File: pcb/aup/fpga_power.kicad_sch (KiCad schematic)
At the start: 1 part, among them U1 XC7A50T-FGG484

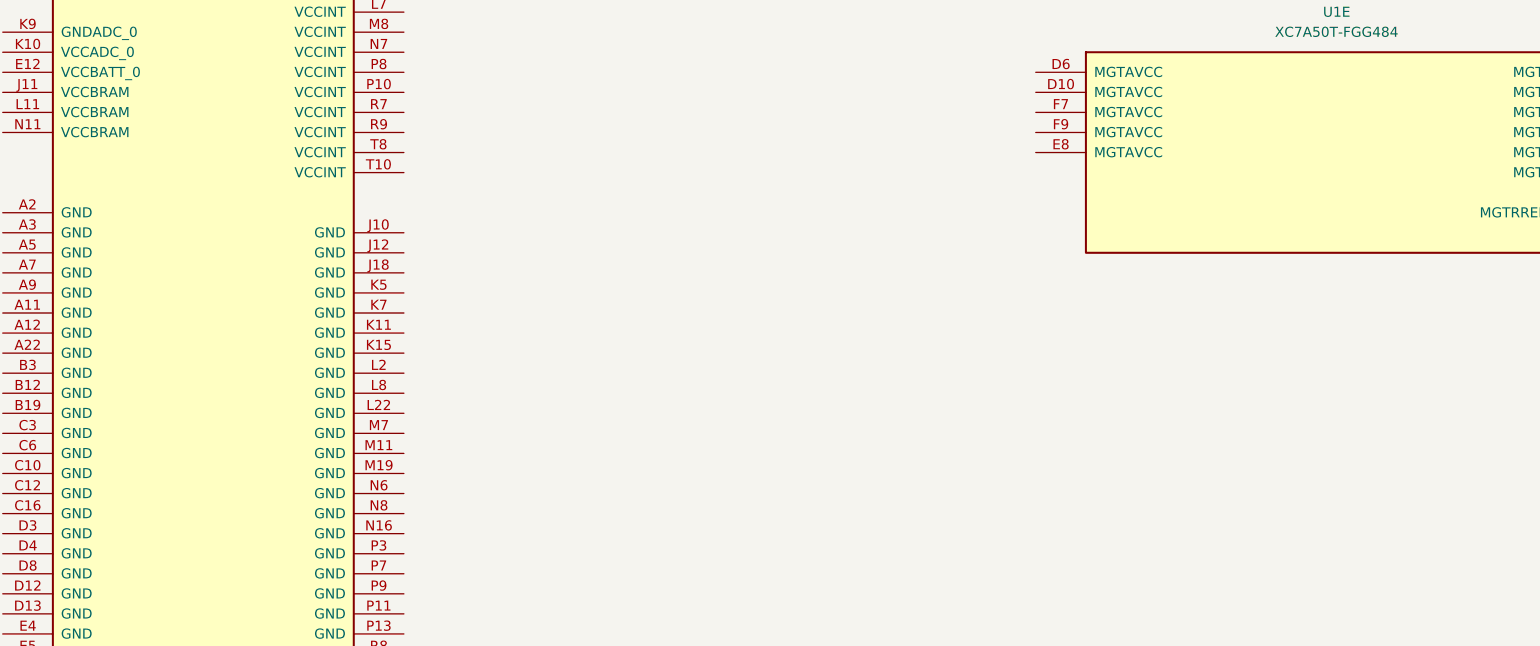
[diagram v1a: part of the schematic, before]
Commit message: Relative path fixes
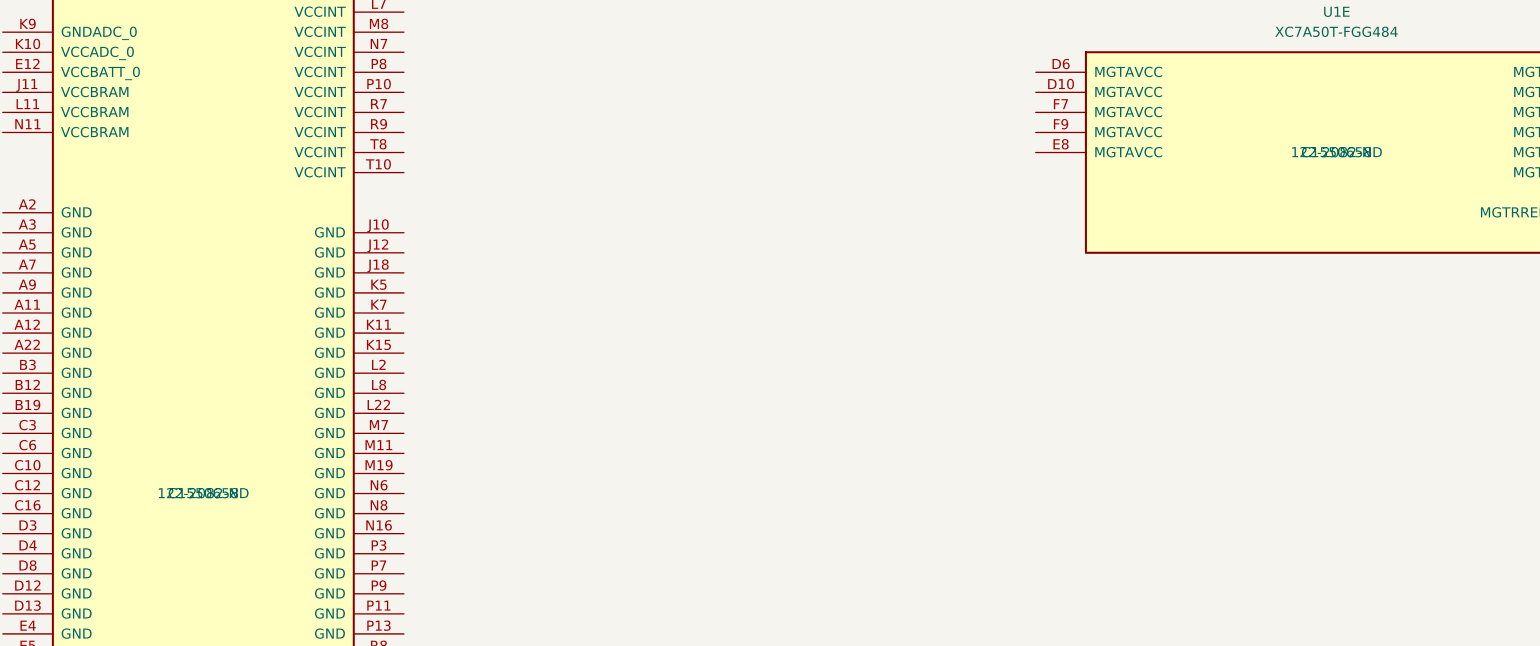
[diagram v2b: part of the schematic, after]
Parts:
- U1: footprint Package_BGA:Xilinx_FGG484 -> !Xilinx:Xilinx_FGG484; Digi-Key Part Number (none) -> 122-2082-ND; LCSC Part # (none) -> C1550658
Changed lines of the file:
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@@
 			)
 		)
-		(property "Footprint" "Package_BGA:Xilinx_FGG484"
+		(property "Footprint" "!Xilinx:Xilinx_FGG484"
 			(at 210.82 54.61 0)
 			(effects
@@
 			)
 		)
-		(property "Description" "Artix 7 T 50 XC7A50T-FGG484"
+		(property "Description" "XC7A50T-2FGG484C"
 			(at 210.82 54.61 0)
 			(effects
@@
 				)
 				(hide yes)
+			)
+		)
+		(property "LCSC Part #" "C1550658"
+			(at 210.82 54.61 0)
+			(effects
+				(font
+					(size 1.27 1.27)
+				)
+			)
+		)
+		(property "Digi-Key Part Number" "122-2082-ND"
+			(at 210.82 54.61 0)
+			(effects
+				(font
+					(size 1.27 1.27)
+				)
 			)
 		)
@@
 			)
 		)
-		(property "Footprint" "Package_BGA:Xilinx_FGG484"
+		(property "Footprint" "!Xilinx:Xilinx_FGG484"
 			(at 67.31 97.79 0)
 			(effects
@@
 			)
 		)
-		(property "Description" "Artix 7 T 50 XC7A50T-FGG484"
+		(property "Description" "XC7A50T-2FGG484C"
 			(at 67.31 97.79 0)
 			(effects
@@
 			)
 		)
+		(property "LCSC Part #" "C1550658"
+			(at 67.31 97.79 0)
+			(effects
+				(font
+					(size 1.27 1.27)
+				)
+			)
+		)
+		(property "Digi-Key Part Number" "122-2082-ND"
+			(at 67.31 97.79 0)
+			(effects
+				(font
+					(size 1.27 1.27)
+				)
+			)
+		)

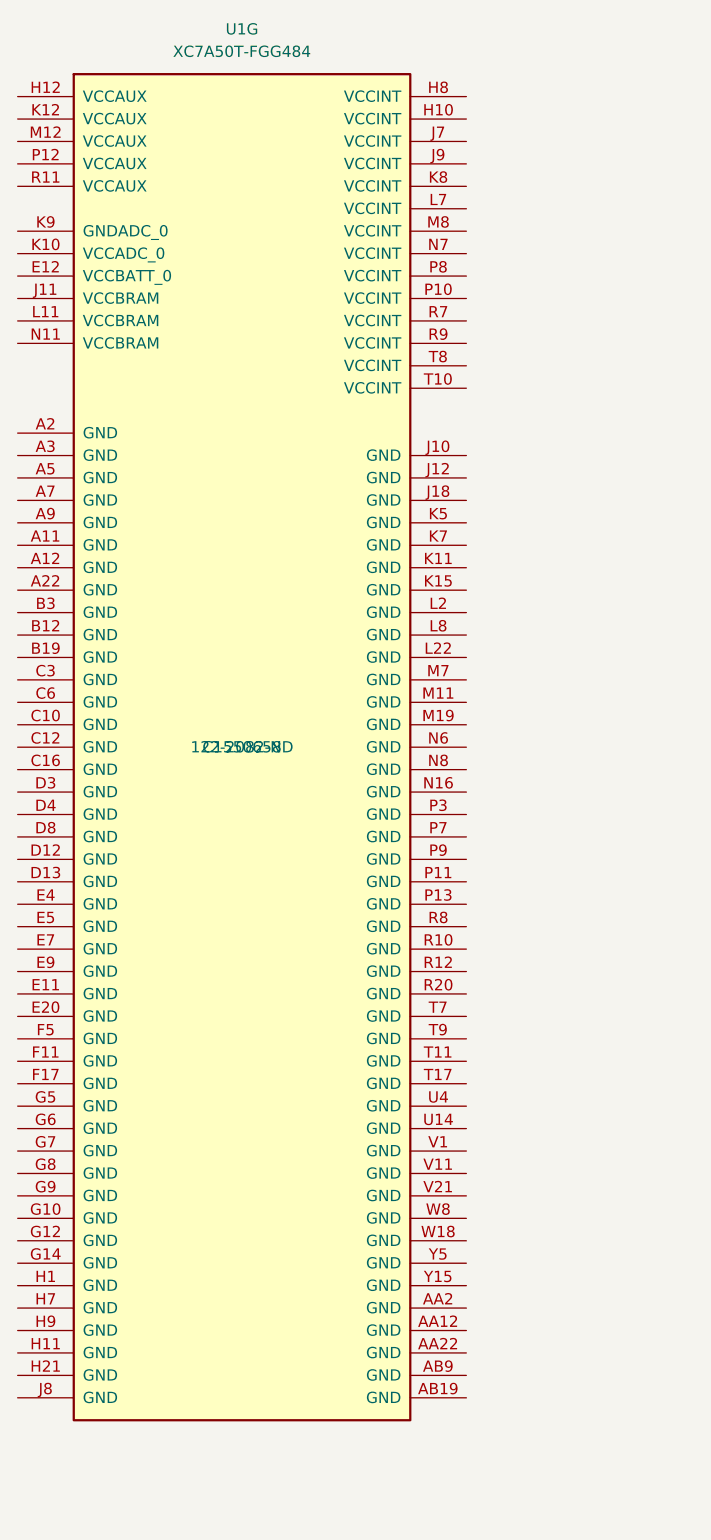
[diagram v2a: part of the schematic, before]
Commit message: Add some todo's on schematic. Add vias to fpga
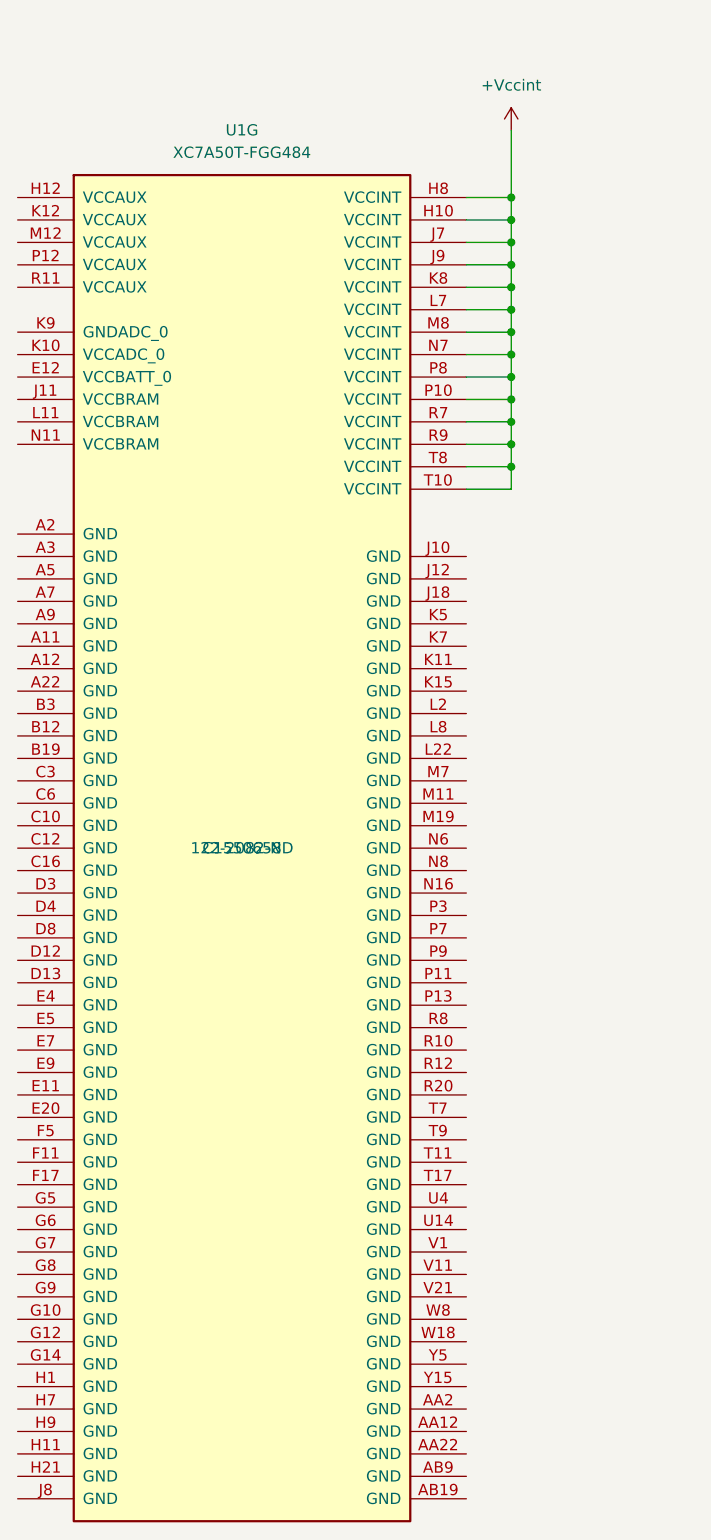
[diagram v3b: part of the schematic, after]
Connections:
- net +Vccint: now reaches U1.H10 (VCCINT)
- net +Vccint: now also U1.H8 (VCCINT), U1.J7 (VCCINT), U1.J9 (VCCINT), U1.K8 (VCCINT), U1.L7 (VCCINT), U1.M8 (VCCINT), U1.N7 (VCCINT), U1.P10 (VCCINT), U1.P8 (VCCINT), U1.R7 (VCCINT), U1.R9 (VCCINT), U1.T10 (VCCINT), U1.T8 (VCCINT)
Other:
- moved on the sheet: U1G

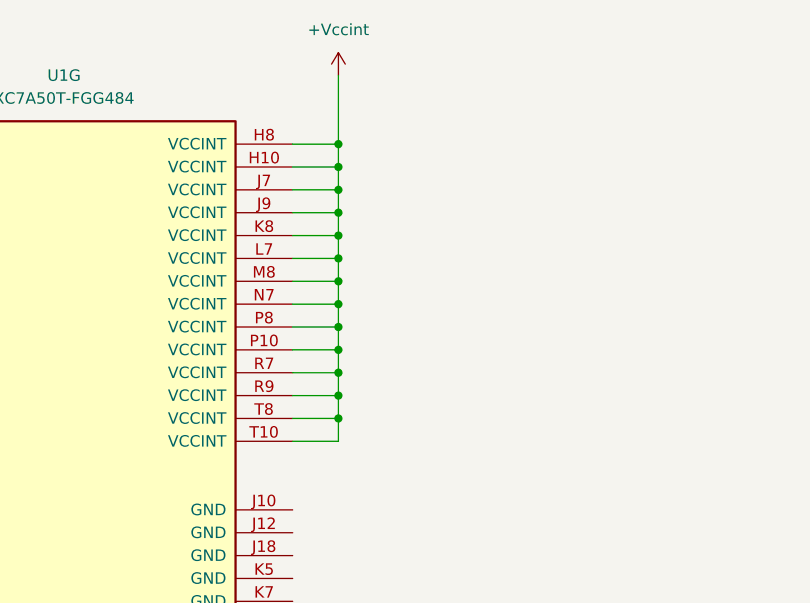
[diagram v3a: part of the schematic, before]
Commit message: Start to add net class color
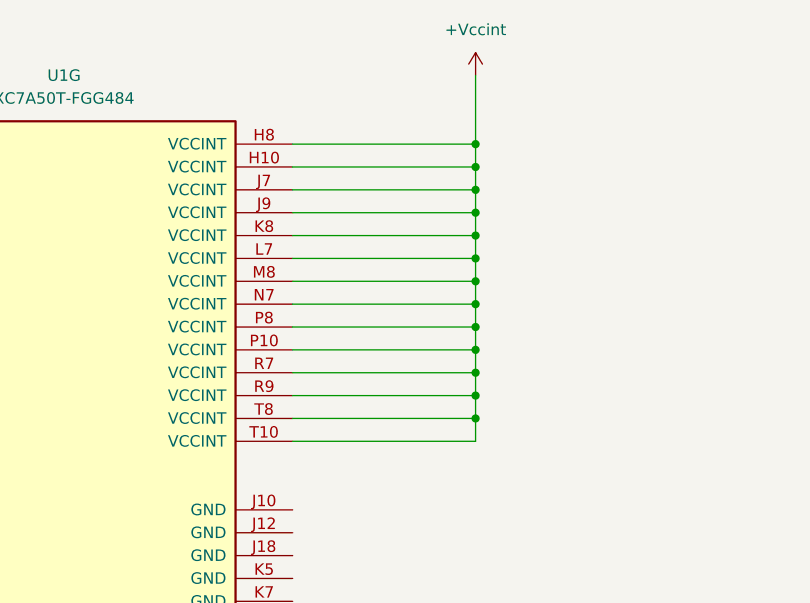
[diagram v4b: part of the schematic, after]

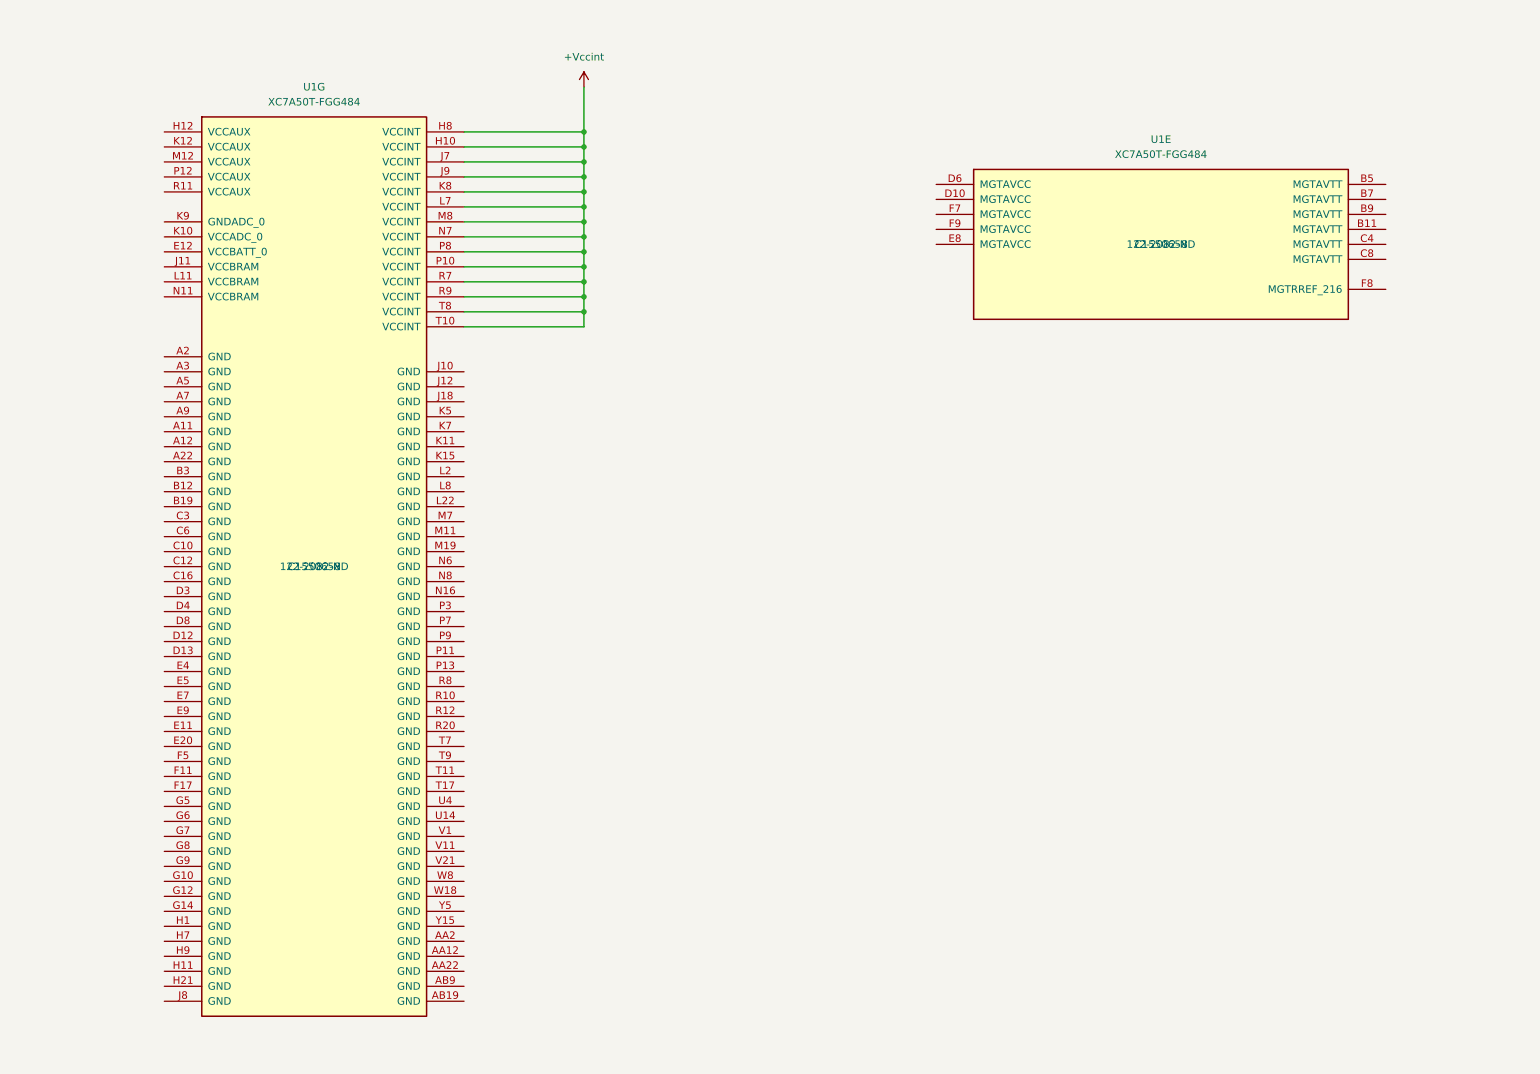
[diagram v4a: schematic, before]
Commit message: Add netnames for rails
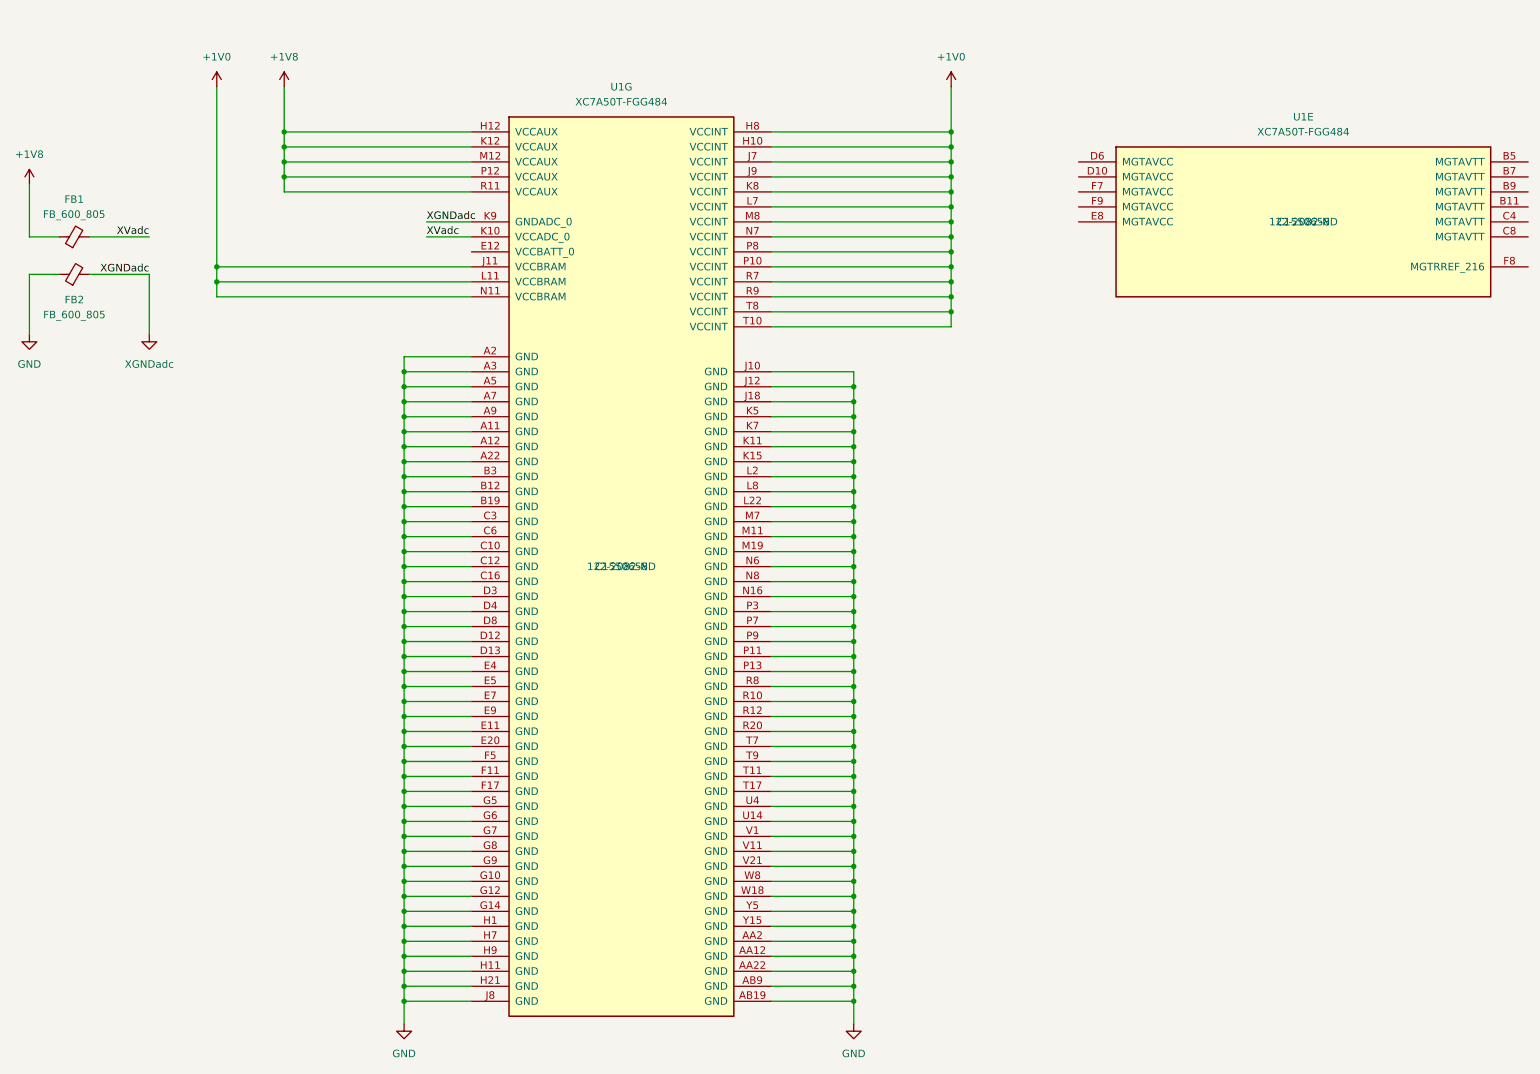
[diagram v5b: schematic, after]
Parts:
- added FB1, FB2: FB_600_805, Inductor_SMD:L_0805_2012Metric, symbol !Misc:FB_600
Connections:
- net +Vccint is gone; now on net +1V0: U1.H10 (VCCINT), U1.H8 (VCCINT), U1.J7 (VCCINT), U1.J9 (VCCINT), U1.K8 (VCCINT), U1.L7 (VCCINT), U1.M8 (VCCINT), U1.N7 (VCCINT), U1.P10 (VCCINT), U1.P8 (VCCINT), U1.R7 (VCCINT), U1.R9 (VCCINT), U1.T10 (VCCINT), U1.T8 (VCCINT)
- net GND: now reaches U1.A11 (GND)
- net GND: now also U1.A12 (GND), U1.A2 (GND), U1.A22 (GND), U1.A3 (GND), U1.A5 (GND), U1.A7 (GND), U1.A9 (GND), U1.AA12 (GND), U1.AA2 (GND), U1.AA22 (GND), U1.AB19 (GND), U1.AB9 (GND), U1.B12 (GND), U1.B19 (GND), U1.B3 (GND), U1.C10 (GND), U1.C12 (GND), U1.C16 (GND), U1.C3 (GND), U1.C6 (GND), U1.D12 (GND), U1.D13 (GND), U1.D3 (GND), U1.D4 (GND), U1.D8 (GND), U1.E11 (GND), U1.E20 (GND), U1.E4 (GND), U1.E5 (GND), U1.E7 (GND), U1.E9 (GND), U1.F11 (GND), U1.F17 (GND), U1.F5 (GND), U1.G10 (GND), U1.G12 (GND), U1.G14 (GND), U1.G5 (GND), U1.G6 (GND), U1.G7 (GND), U1.G8 (GND), U1.G9 (GND), U1.H1 (GND), U1.H11 (GND), U1.H21 (GND), U1.H7 (GND), U1.H9 (GND), U1.J10 (GND), U1.J12 (GND), U1.J18 (GND), U1.J8 (GND), U1.K11 (GND), U1.K15 (GND), U1.K5 (GND), U1.K7 (GND), U1.L2 (GND), U1.L22 (GND), U1.L8 (GND), U1.M11 (GND), U1.M19 (GND), U1.M7 (GND), U1.N16 (GND), U1.N6 (GND), U1.N8 (GND), U1.P11 (GND), U1.P13 (GND), U1.P3 (GND), U1.P7 (GND), U1.P9 (GND), U1.R10 (GND), U1.R12 (GND), U1.R20 (GND), U1.R8 (GND), U1.T11 (GND), U1.T17 (GND), U1.T7 (GND), U1.T9 (GND), U1.U14 (GND), U1.U4 (GND), U1.V1 (GND), U1.V11 (GND), U1.V21 (GND), U1.W18 (GND), U1.W8 (GND), U1.Y15 (GND), U1.Y5 (GND), FB2.1
- net +1V8: now reaches U1.H12 (VCCAUX)
- net +1V8: now also U1.K12 (VCCAUX), U1.M12 (VCCAUX), U1.P12 (VCCAUX), U1.R11 (VCCAUX), FB1.1
- net +1V0: now reaches U1.J11 (VCCBRAM)
- net +1V0: now also U1.L11 (VCCBRAM), U1.N11 (VCCBRAM)
- net XVadc: now reaches U1.K10 (VCCADC_0)
- net XVadc: now also FB1.2
- net XGNDadc: now reaches U1.K9 (GNDADC_0)
- net XGNDadc: now also FB2.2
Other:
- moved on the sheet: U1E, U1G
